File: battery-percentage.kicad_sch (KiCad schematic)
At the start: 11 parts, among them J1 Conn_01x04_Pin, SW1 SW_Push, U1 WeMos_D1_mini, U2 LM7805_TO220

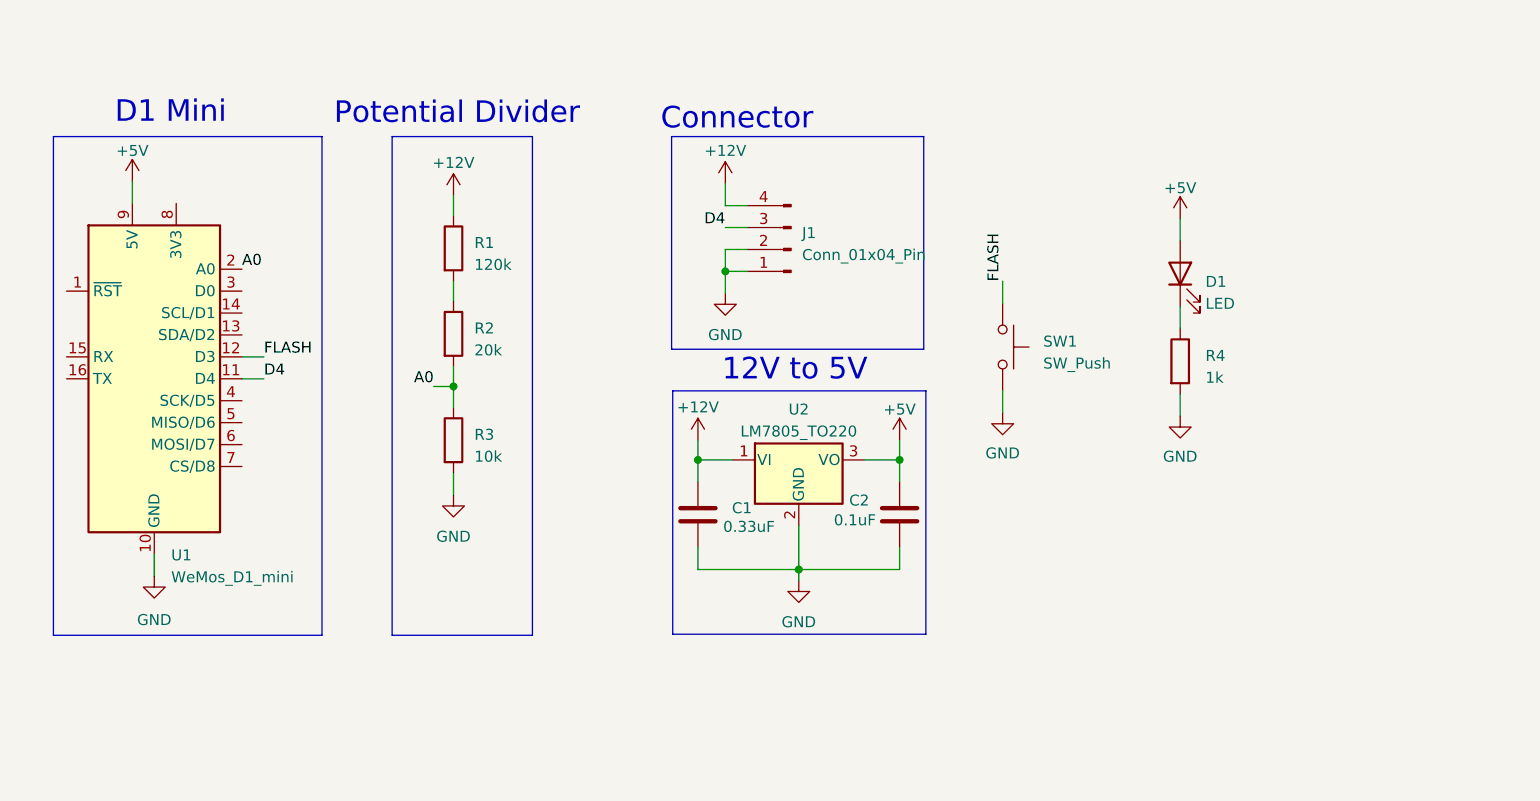
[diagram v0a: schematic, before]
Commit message: Added TTl Interface to Schematic
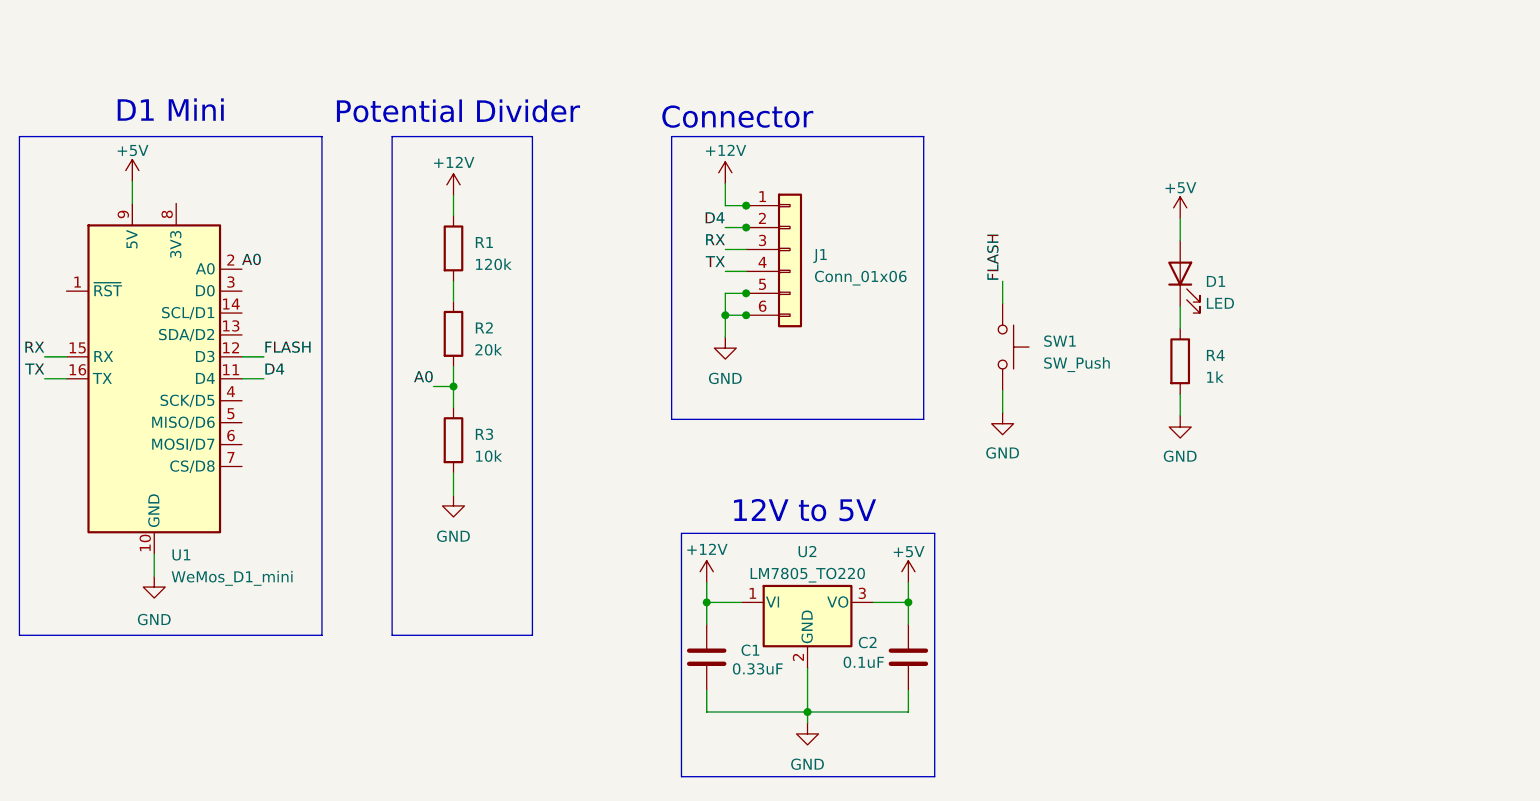
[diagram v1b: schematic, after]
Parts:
- removed J1: Conn_01x04_Pin, Connector_PinHeader_2.00mm:PinHeader_1x04_P2.00mm_Horizontal, symbol Connector:Conn_01x04_Pin
- added J1: Conn_01x06, Connector_PinHeader_2.00mm:PinHeader_1x06_P2.00mm_Horizontal, symbol Connector_Generic:Conn_01x06
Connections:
- net +12V: now also J1.1 (Pin_1)
- net D4: now also J1.2 (Pin_2)
- net GND: now also J1.5 (Pin_5), J1.6 (Pin_6)
- net RX: now reaches U1.15 (RX)
- net RX: now also J1.3 (Pin_3)
- net TX: now reaches U1.16 (TX)
- net TX: now also J1.4 (Pin_4)
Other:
- moved on the sheet: C1, C2, U2

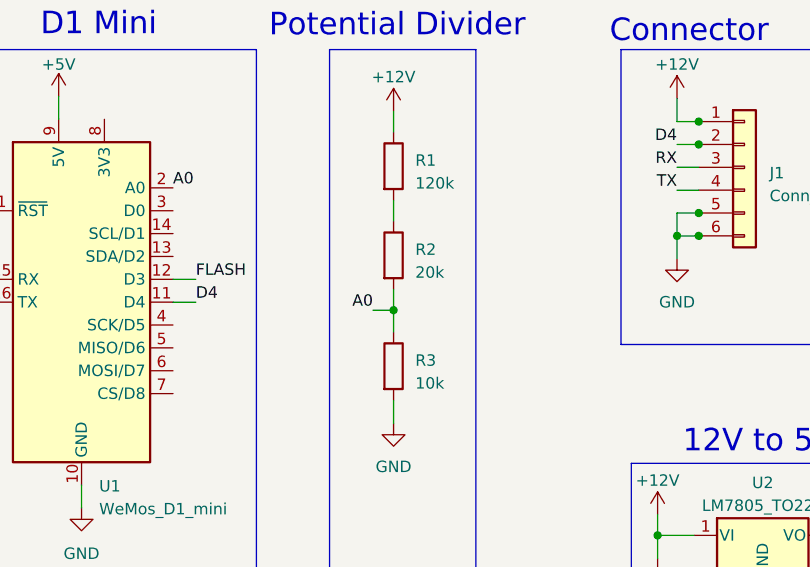
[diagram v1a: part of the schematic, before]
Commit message: Updated Potential Divider
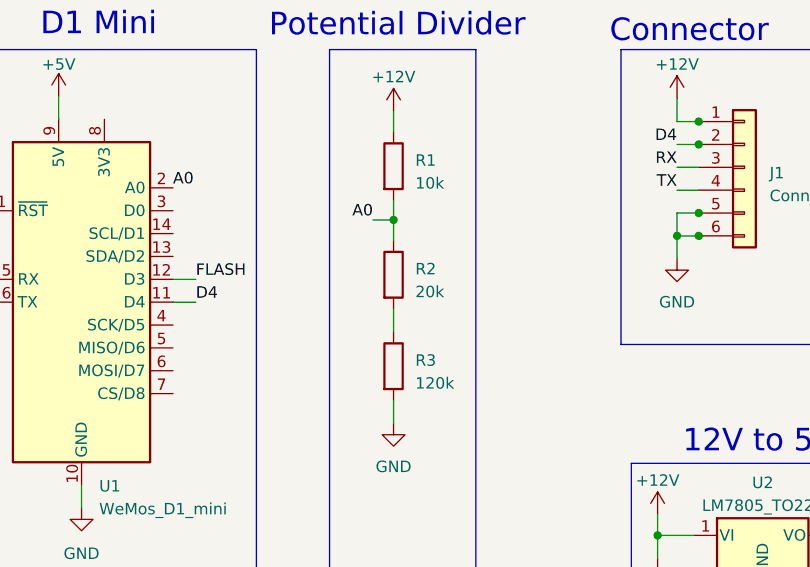
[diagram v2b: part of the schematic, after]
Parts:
- R1: value 120k -> 10k
- R3: value 10k -> 120k
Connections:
- net A0: now also R1.2, R2.1; no longer R2.2, R3.1
- new net: R2.2, R3.1
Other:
- moved on the sheet: R2
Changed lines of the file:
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@@
 (kicad_sch (version 20230121) (generator eeschema)
   (paper "A5")
+  (junction (at 71.247 45.593) (diameter 0) (color 0 0 0 0)
+  )
   (junction (at 105.156 47.371) (diameter 0) (color 0 0 0 0)
   )
@@
   (junction (at 105.156 34.671) (diameter 0) (color 0 0 0 0)
   )
-  (junction (at 71.247 55.626) (diameter 0) (color 0 0 0 0)
-  )
   (wire (pts (xy 112.268 93.345) (xy 112.268 94.615))
     (stroke (width 0) (type default))
   )
+  (wire (pts (xy 71.247 45.593) (xy 71.247 47.879))
+    (stroke (width 0) (type default))
+  )
   (wire (pts (xy 105.283 34.671) (xy 105.156 34.671))
     (stroke (width 0) (type default))
   )
+  (wire (pts (xy 71.247 43.434) (xy 71.247 45.593))
+    (stroke (width 0) (type default))
+  )
   (wire (pts (xy 71.247 68.199) (xy 71.247 65.659))
     (stroke (width 0) (type default))
@@
     (stroke (width 0) (type default))
   )
-  (wire (pts (xy 71.247 43.434) (xy 71.247 45.72))
-    (stroke (width 0) (type default))
-  )
   (wire (pts (xy 123.952 80.645) (xy 123.952 78.359))
     (stroke (width 0) (type default))
@@
     (stroke (width 0) (type default))
   )
-  (wire (pts (xy 68.961 55.626) (xy 71.247 55.626))
-    (stroke (width 0) (type default))
-  )
   (wire (pts (xy 49.276 52.197) (xy 46.736 52.197))
     (stroke (width 0) (type default))
@@
     (stroke (width 0) (type default))
   )
-  (wire (pts (xy 71.247 53.34) (xy 71.247 55.626))
-    (stroke (width 0) (type default))
-  )
   (wire (pts (xy 34.036 31.877) (xy 34.036 34.417))
     (stroke (width 0) (type default))
@@
     (stroke (width 0) (type default))
   )
-  (wire (pts (xy 71.247 55.626) (xy 71.247 58.039))
+  (wire (pts (xy 71.247 55.499) (xy 71.247 58.039))
     (stroke (width 0) (type default))
   )
   (wire (pts (xy 100.584 80.645) (xy 104.648 80.645))
+    (stroke (width 0) (type default))
+  )
+  (wire (pts (xy 68.961 45.593) (xy 71.247 45.593))
     (stroke (width 0) (type default))
   )
@@
     (effects (font (size 2.5 2.5)) (justify left bottom))
   )
-  (label "A0" (at 68.961 55.626 180) (fields_autoplaced)
-    (effects (font (size 1.27 1.27)) (justify right bottom))
-  )
   (label "TX" (at 23.876 54.737 180) (fields_autoplaced)
     (effects (font (size 1.27 1.27)) (justify right bottom))
@@
     (effects (font (size 1.27 1.27)) (justify right bottom))
   )
+  (label "A0" (at 68.961 45.593 180) (fields_autoplaced)
+    (effects (font (size 1.27 1.27)) (justify right bottom))
+  )
   (label "TX" (at 102.743 42.291 180) (fields_autoplaced)
     (effects (font (size 1.27 1.27)) (justify right bottom))
@@
     )
   )
-  (symbol (lib_id "Device:R") (at 71.247 49.53 0) (unit 1)
-    (in_bom yes) (on_board yes) (dnp no) (fields_autoplaced)
-    (property "Reference" "R2" (at 73.66 48.895 0)
-      (effects (font (size 1.27 1.27)) (justify left))
-    )
-    (property "Value" "20k" (at 73.66 51.435 0)
-      (effects (font (size 1.27 1.27)) (justify left))
-    )
-    (property "Footprint" "Resistor_THT:R_Axial_DIN0204_L3.6mm_D1.6mm_P5.08mm_Horizontal" (at 69.469 49.53 90)
-      (effects (font (size 1.27 1.27)) hide)
-    )
-    (property "Datasheet" "~" (at 71.247 49.53 0)
+  (symbol (lib_id "Device:R") (at 71.247 51.689 0) (unit 1)
+    (in_bom yes) (on_board yes) (dnp no) (fields_autoplaced)
+    (property "Reference" "R2" (at 73.66 51.054 0)
+      (effects (font (size 1.27 1.27)) (justify left))
+    )
+    (property "Value" "20k" (at 73.66 53.594 0)
+      (effects (font (size 1.27 1.27)) (justify left))
+    )
+    (property "Footprint" "Resistor_THT:R_Axial_DIN0204_L3.6mm_D1.6mm_P5.08mm_Horizontal" (at 69.469 51.689 90)
+      (effects (font (size 1.27 1.27)) hide)
+    )
+    (property "Datasheet" "~" (at 71.247 51.689 0)
       (effects (font (size 1.27 1.27)) hide)
     )
@@
       (effects (font (size 1.27 1.27)) (justify left))
     )
-    (property "Value" "10k" (at 73.66 63.754 0)
+    (property "Value" "120k" (at 73.66 63.754 0)
       (effects (font (size 1.27 1.27)) (justify left))
     )
@@
       (effects (font (size 1.27 1.27)) (justify left))
     )
-    (property "Value" "120k" (at 73.66 41.529 0)
-      (effects (font (size 1.27 1.27)) (justify left))
-    )
+    (property "Value" "10k" (at 73.66 41.529 0)
+      (effects (font (size 1.27 1.27)) (justify left))
+    )

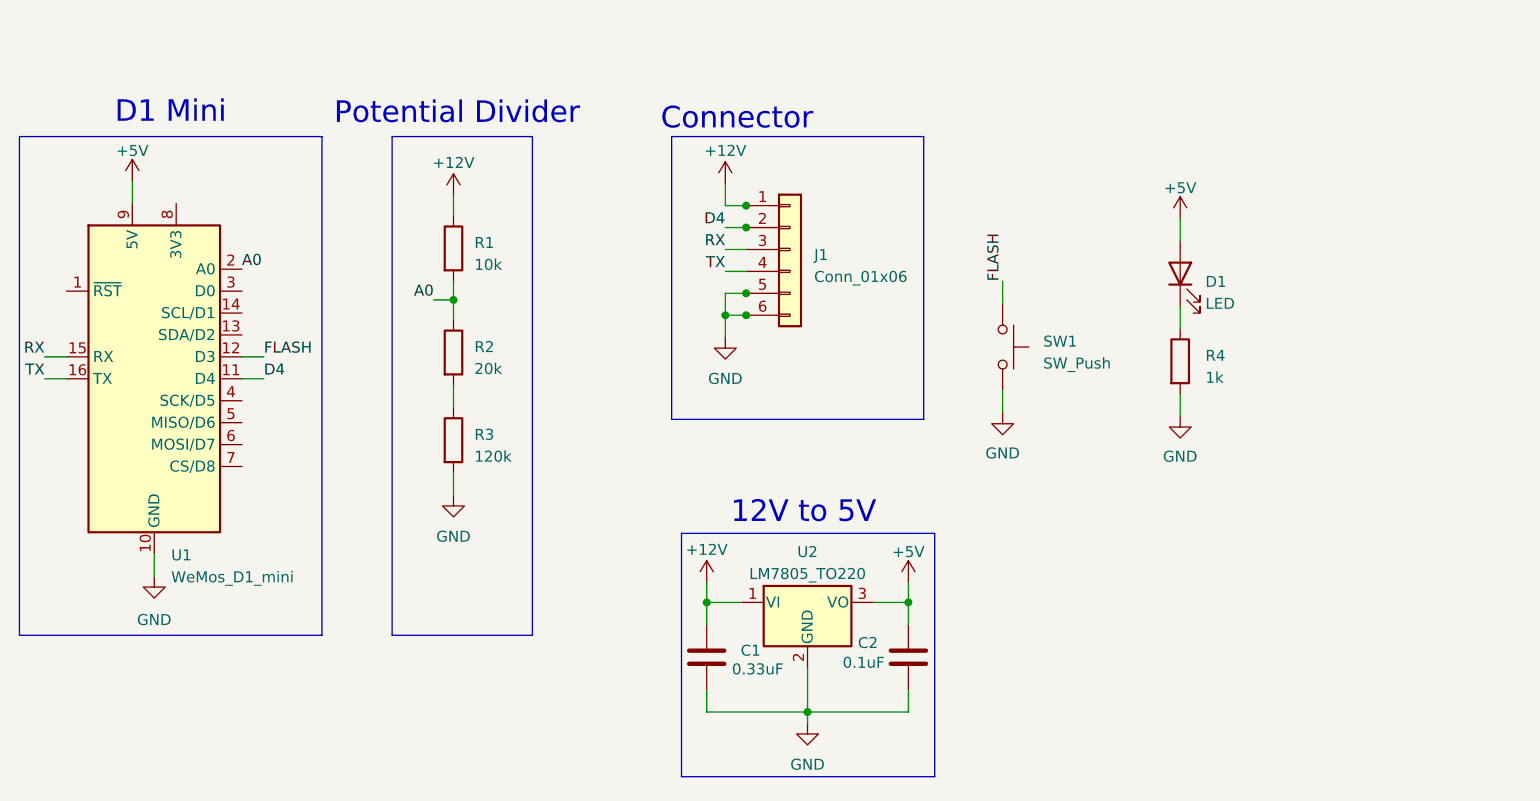
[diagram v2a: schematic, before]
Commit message: Updated Potential Divider & Capacitor
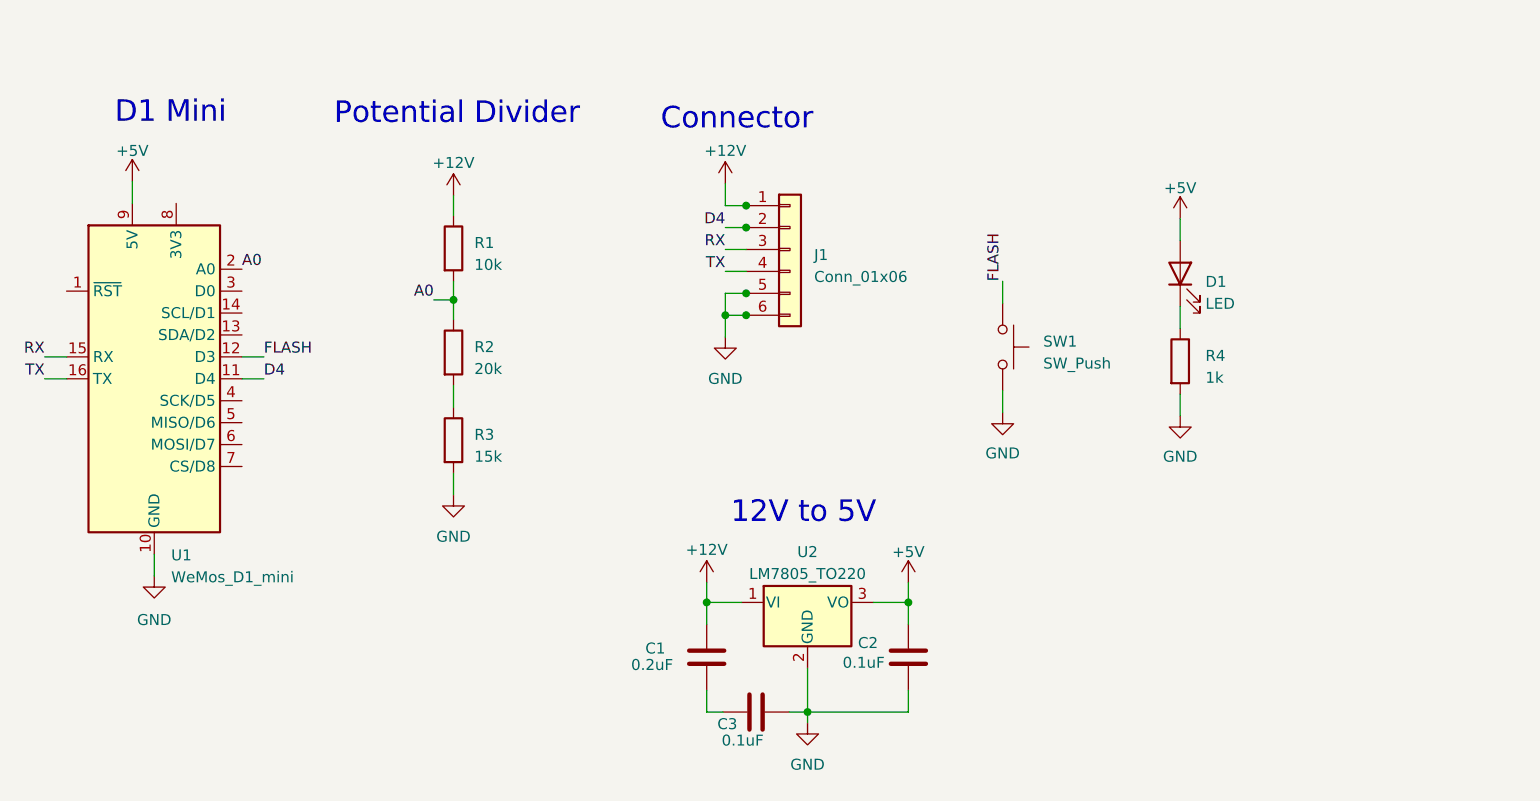
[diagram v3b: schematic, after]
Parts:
- added C3: 0.1uF, Capacitor_THT:CP_Radial_D4.0mm_P1.50mm, symbol Device:C
- C1: value 0.33uF -> 0.2uF
- R3: value 120k -> 15k
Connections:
- net GND: now also C3.2; no longer C1.2
- new net: C1.2, C3.1
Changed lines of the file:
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@@
+    (stroke (width 0) (type default))
+  )
+  (wire (pts (xy 110.109 93.345) (xy 112.268 93.345))
     (stroke (width 0) (type default))
   )
@@
     (stroke (width 0) (type default))
   )
-  (wire (pts (xy 100.584 93.345) (xy 112.268 93.345))
+  (wire (pts (xy 100.584 93.345) (xy 102.489 93.345))
     (stroke (width 0) (type default))
   )
@@
   (wire (pts (xy 102.743 49.911) (xy 102.743 47.371))
     (stroke (width 0) (type default))
-  )
-  (rectangle (start 97.663 72.644) (end 127 100.838)
-    (stroke (width 0) (type default))
-    (fill (type none))
-  )
-  (rectangle (start 20.955 26.67) (end 56.007 84.455)
-    (stroke (width 0) (type default))
-    (fill (type none))
-  )
-  (rectangle (start 64.135 26.67) (end 80.391 84.455)
-    (stroke (width 0) (type default))
-    (fill (type none))
-  )
-  (rectangle (start 96.52 26.67) (end 125.73 59.436)
-    (stroke (width 0) (type default))
-    (fill (type none))
   )
   (text "Potential Divider" (at 57.404 25.527 0)
@@
     )
   )
+  (symbol (lib_id "Device:C") (at 106.299 93.345 90) (unit 1)
+    (in_bom yes) (on_board yes) (dnp no)
+    (property "Reference" "C3" (at 104.14 94.742 90)
+      (effects (font (size 1.27 1.27)) (justify left))
+    )
+    (property "Value" "0.1uF" (at 107.188 96.647 90)
+      (effects (font (size 1.27 1.27)) (justify left))
+    )
+    (property "Footprint" "Capacitor_THT:CP_Radial_D4.0mm_P1.50mm" (at 110.109 92.3798 0)
+      (effects (font (size 1.27 1.27)) hide)
+    )
+    (property "Datasheet" "~" (at 106.299 93.345 0)
+      (effects (font (size 1.27 1.27)) hide)
+    )
+    (pin "1")
+    (pin "2")
+    (instances
+      (project "battery-percentage"
+        (path "/f79966b4-4927-4ec7-886d-17305cb22602"
+          (reference "C3") (unit 1)
+        )
+      )
+    )
+  )
   (symbol (lib_id "power:GND") (at 71.247 68.199 0) (unit 1)
     (in_bom yes) (on_board yes) (dnp no) (fields_autoplaced)
@@
       (effects (font (size 1.27 1.27)) (justify left))
     )
-    (property "Value" "120k" (at 73.66 63.754 0)
+    (property "Value" "15k" (at 73.66 63.754 0)
       (effects (font (size 1.27 1.27)) (justify left))
     )
@@
   (symbol (lib_id "Device:C") (at 100.584 86.995 0) (unit 1)
     (in_bom yes) (on_board yes) (dnp no)
-    (property "Reference" "C1" (at 104.521 86.233 0)
-      (effects (font (size 1.27 1.27)) (justify left))
-    )
-    (property "Value" "0.33uF" (at 103.505 88.392 0)
-      (effects (font (size 1.27 1.27)) (justify left))
-    )
+    (property "Reference" "C1" (at 93.472 85.979 0)
+      (effects (font (size 1.27 1.27)) (justify left))
+    )
+    (property "Value" "0.2uF" (at 91.821 87.884 0)
+      (effects (font (size 1.27 1.27)) (justify left))
+    )
